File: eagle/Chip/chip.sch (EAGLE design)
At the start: 58 parts, among them IC1 MCP604SL, J1 3x4 Keypad, Q1 TRANS_NPN-MMBTA42, Q2 BT137-600E, U1 328P, U2 TRIAC_OPTOCOUPLER-MOC3063SM, U3 SFH6206, Y1 16MHz

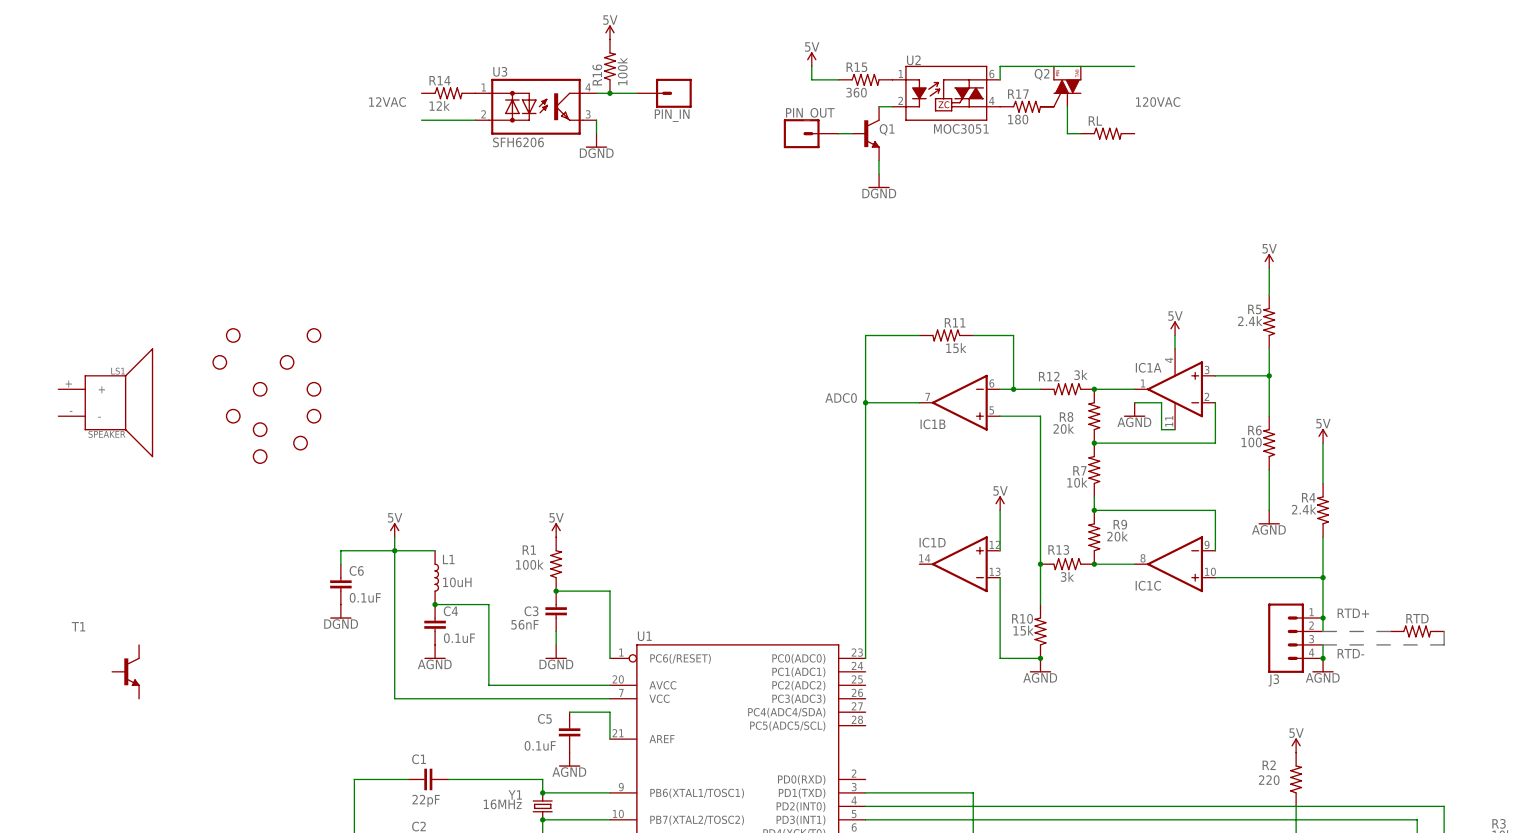
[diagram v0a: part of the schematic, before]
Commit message: added speaker to eagle
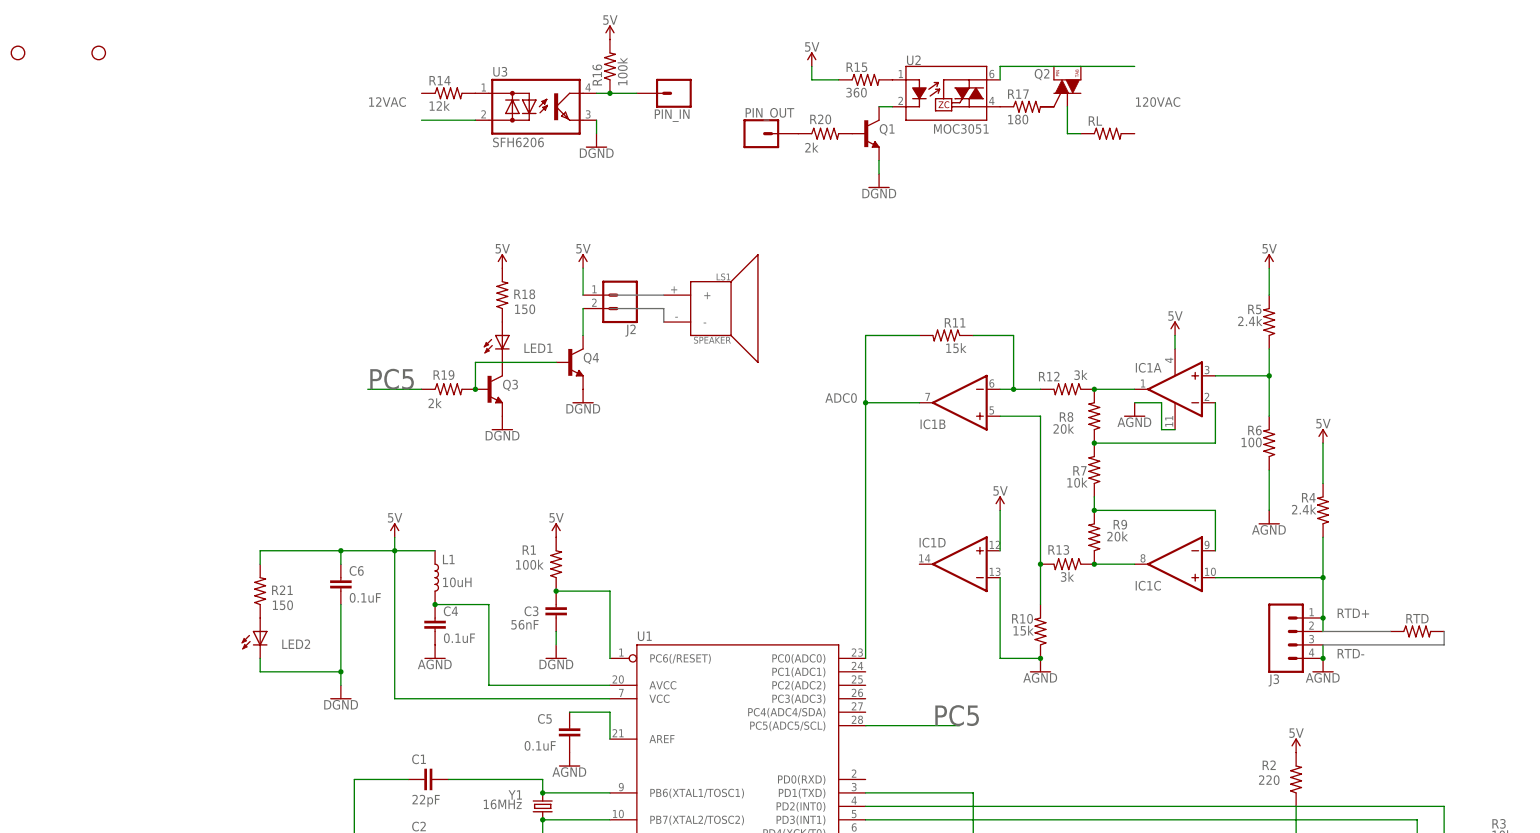
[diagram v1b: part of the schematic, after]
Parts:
- removed H1, H2, H3, H4, H5, H6, H7, H8, H9: STAND-OFF, SparkFun-Hardware:STAND-OFF
- removed T1: (no value), transistor-neu-to92:MMBT3904LT1-NPN-SOT23-BEC
- added J2: (no value), SparkFun-Connectors:CONN_02
- added LED1, LED2: (no value), adafruit:LED5MM
- added Q3, Q4: TRANS_NPN-MMBTA42, SparkFun-DiscreteSemi:TRANS_NPN-MMBTA42
- added R18, R21: 150, adafruit:R-US_R0603
- added R19, R20: 2k, adafruit:R-US_R0603
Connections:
- new net N$38: LED1.C, Q3.C
- new net N$39: LED1.A, R18.1
- new net N$40: Q3.B, Q4.B, R19.2
- new net N$41: PIN_OUT.1, R20.1
- new net N$42: J2.2, Q4.C
- new net N$43: R19.1
- new net N$44: U1.PC5(ADC5/SCL)
- new net N$45: LED2.A, R21.1
- net 5V: now also J2.1, R18.2, R21.2
- net GND: now also LED2.C, Q3.E, Q4.E
- net N$35: now also R20.2; no longer PIN_OUT.1
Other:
- note added: "PC5"
- moved on the sheet: LS1, PIN_OUT

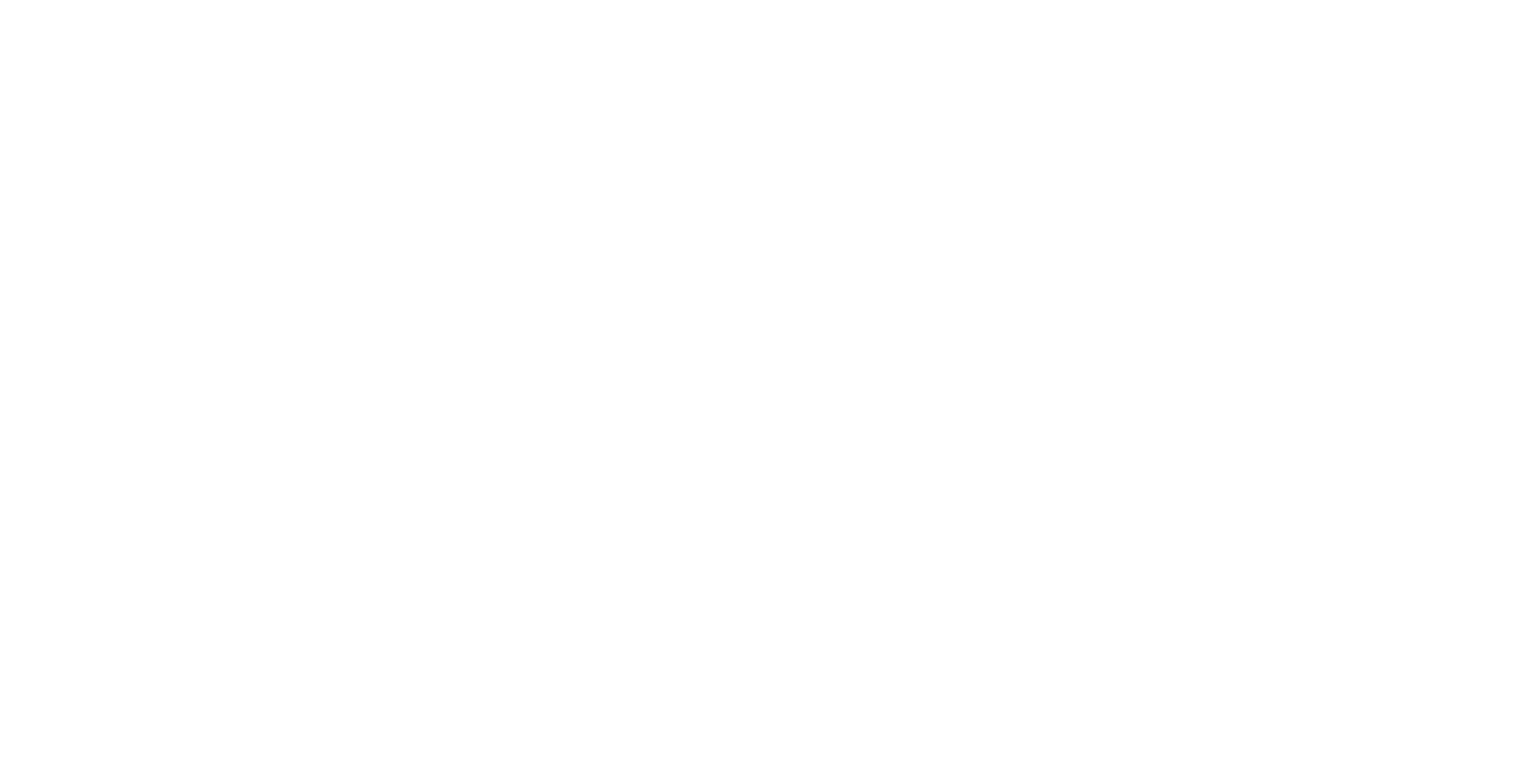
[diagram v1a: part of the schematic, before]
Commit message: Created custom XFMR in eagle
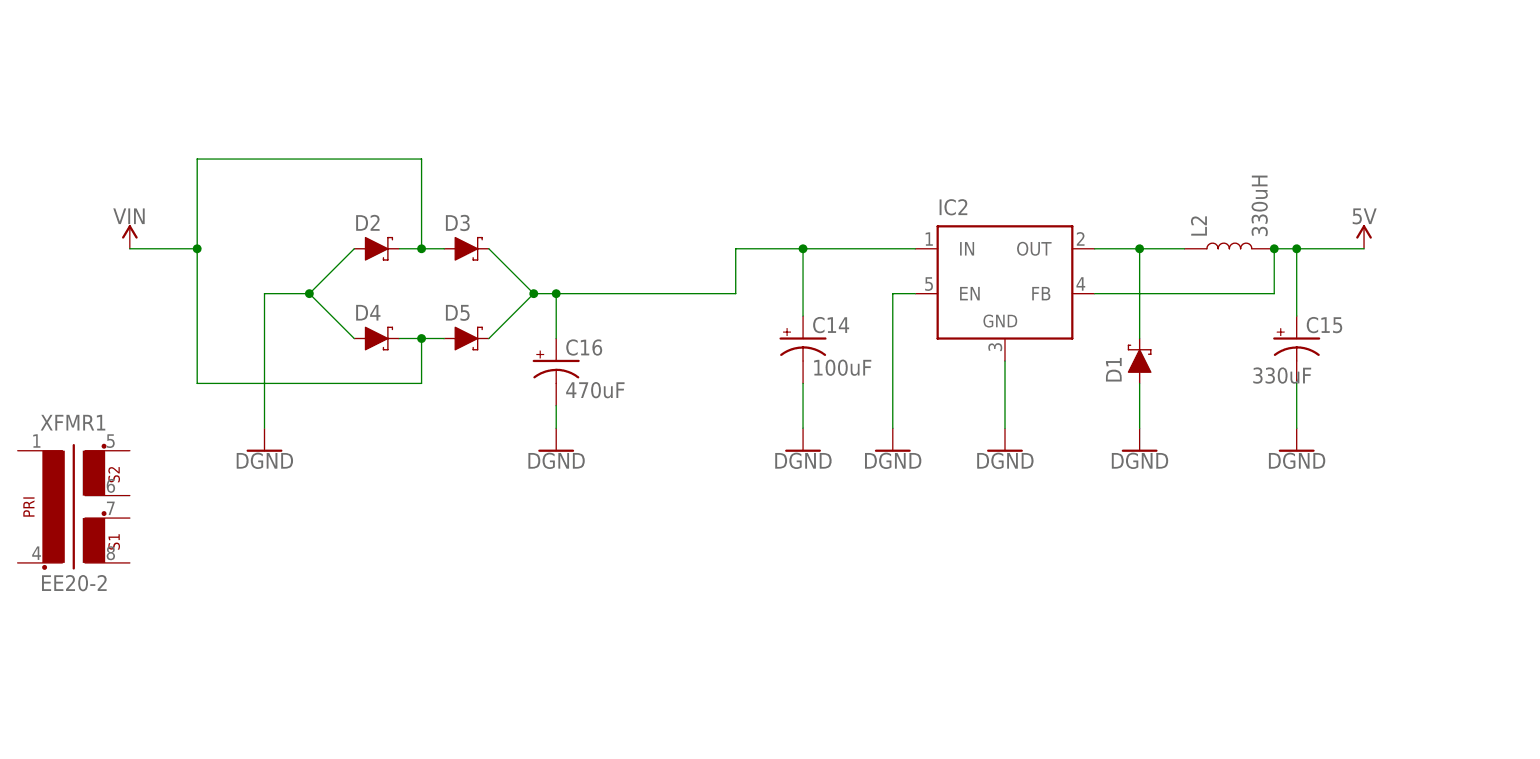
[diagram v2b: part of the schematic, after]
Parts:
- added C14: 100uF, SparkFun-Capacitors:100UF-POLAR-RADIAL-2.5MM-25V-20%
- added C15: 47UF-POLAR-PANASONIC_D-50V-20%, SparkFun-Capacitors:47UF-POLAR-PANASONIC_D-50V-20%
- added C16: 470uF, SparkFun-Capacitors:47UF-POLAR-PANASONIC_D-35V-20%
- added D1, D2, D3, D4, D5: DIODE-SCHOTTKY-B340A, SparkFun-DiscreteSemi:DIODE-SCHOTTKY-B340A
- added IC2: (no value), linear:LM2596TH
- added L2: 330uH, SparkFun-Coils:INDUCTOR-CR75-68UH
- added XFMR1: EE20-2, ece:EE20-2
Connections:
- new net N$46: D1.C, IC2.OUT, L2.1
- new net N$47: C14.+, C16.+, D3.C, D5.C, IC2.IN
- new net N$48: C14.-
- new net VIN: D2.C, D3.A, D4.C, D5.A
- net 5V: now also C15.+, IC2.FB, L2.2
- net GND: now also C15.-, C16.-, D1.A, D2.A, D4.A, IC2.EN, IC2.GND
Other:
- note added: "330uF"
